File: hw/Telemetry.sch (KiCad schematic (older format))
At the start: 31 parts, among them J101 BOOT0, J102 BOOT0, J103 SPORT, J104 SBUS, J105 USB_B_Micro, J106 UART_EXP, SW101 SW_Push, U101 STM32F303CBx, U102 IS25LP032D, X101 SG-310_SCF_8.000000MHZ

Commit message: Updates to board revision 0.2 and newer HAL version
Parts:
- removed J101: BOOT0, Pin_Headers:Pin_Header_Straight_1x02_Pitch1.27mm, symbol Connector_Generic:Conn_01x02
- removed R104: 10k, Resistors_SMD:R_0603_HandSoldering, symbol Device:R_Small
- added R105: 1k5, digikey-footprints:0603, symbol Device:R_Small
- J106: footprint Pin_Headers:Pin_Header_Straight_1x04 -> Connector_PinSocket_1.27mm:PinSocket_1x04_P1.27mm_Vertical
- U101: symbol Misc:STM32F303CBx -> Telemetry-rescue:STM32F303CBx-Misc
- U102: symbol Misc:IS25LP032D -> Telemetry-rescue:IS25LP032D-Misc
- X101: symbol Misc:SG-310_SCF_8.000000MHZ -> Telemetry-rescue:SG-310_SCF_8.000000MHZ-Misc
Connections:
- net labels added: USB_ENUMRATION
- net labels removed: COOLING_TEMP, SERVO_3, SERVO_4
- wire segments 151 -> 149
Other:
- moved on the sheet: J105, J106

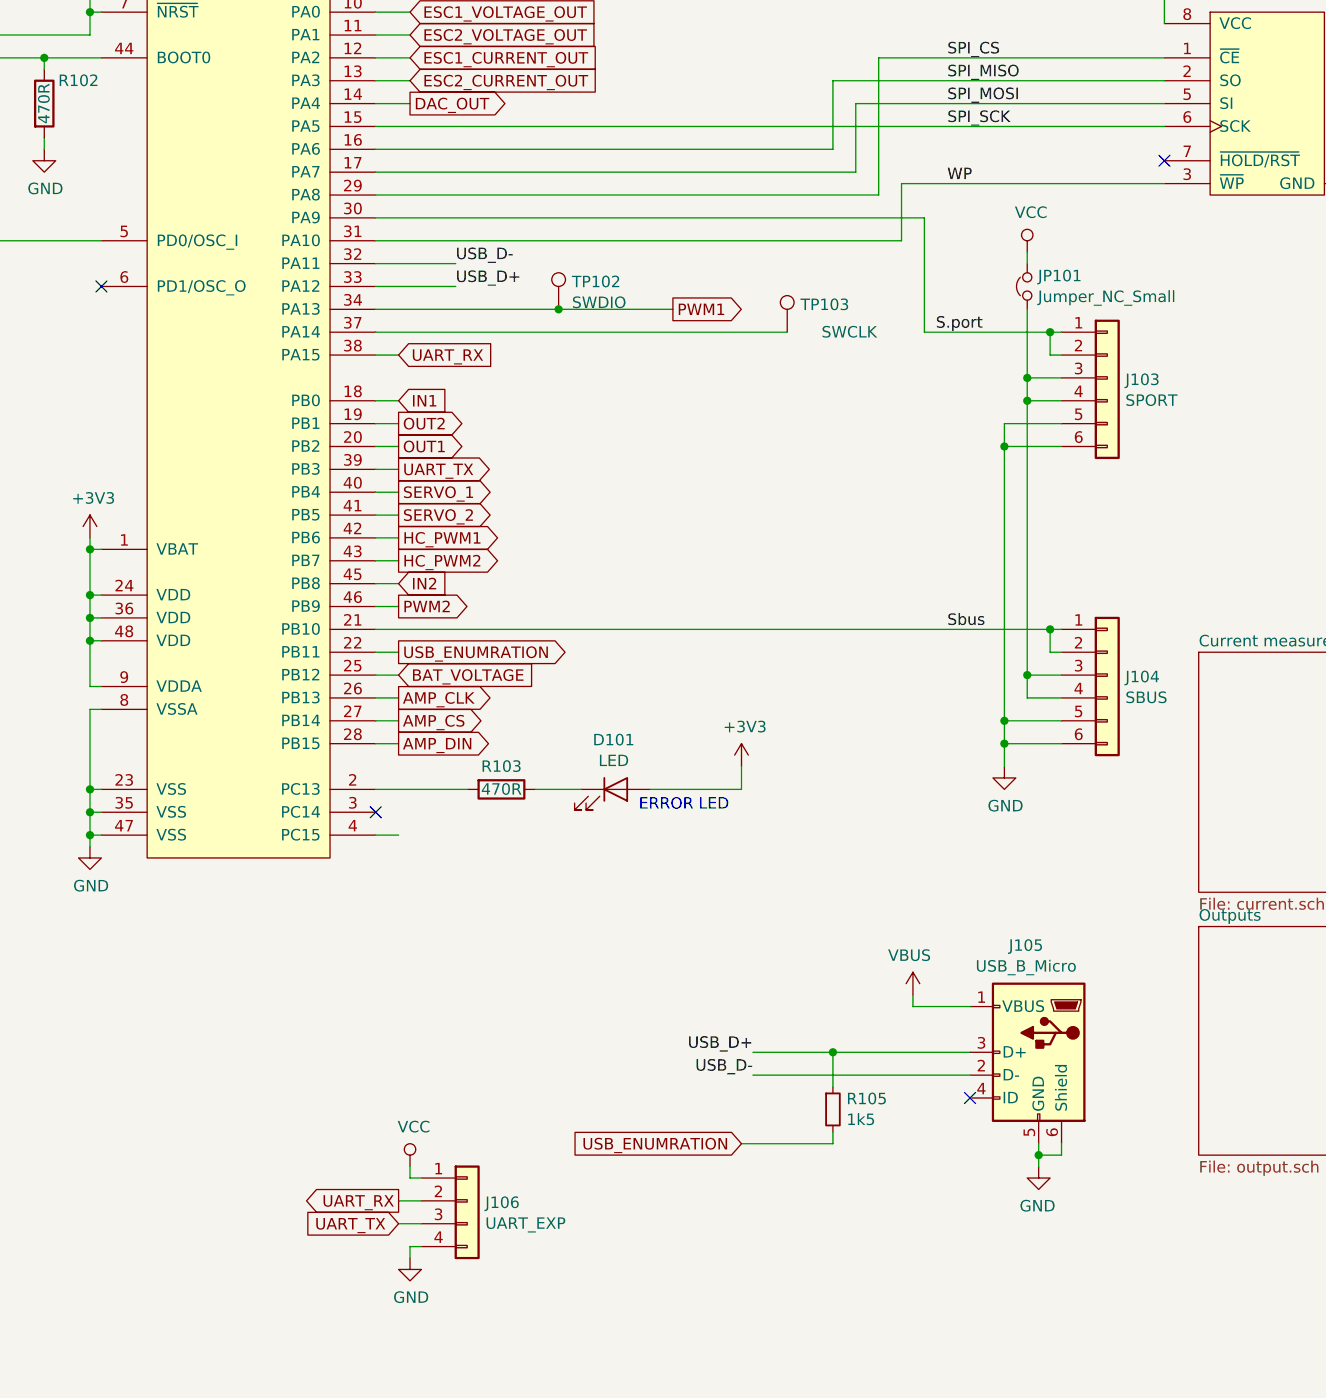
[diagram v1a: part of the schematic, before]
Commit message: Pin remapping and layout improvements
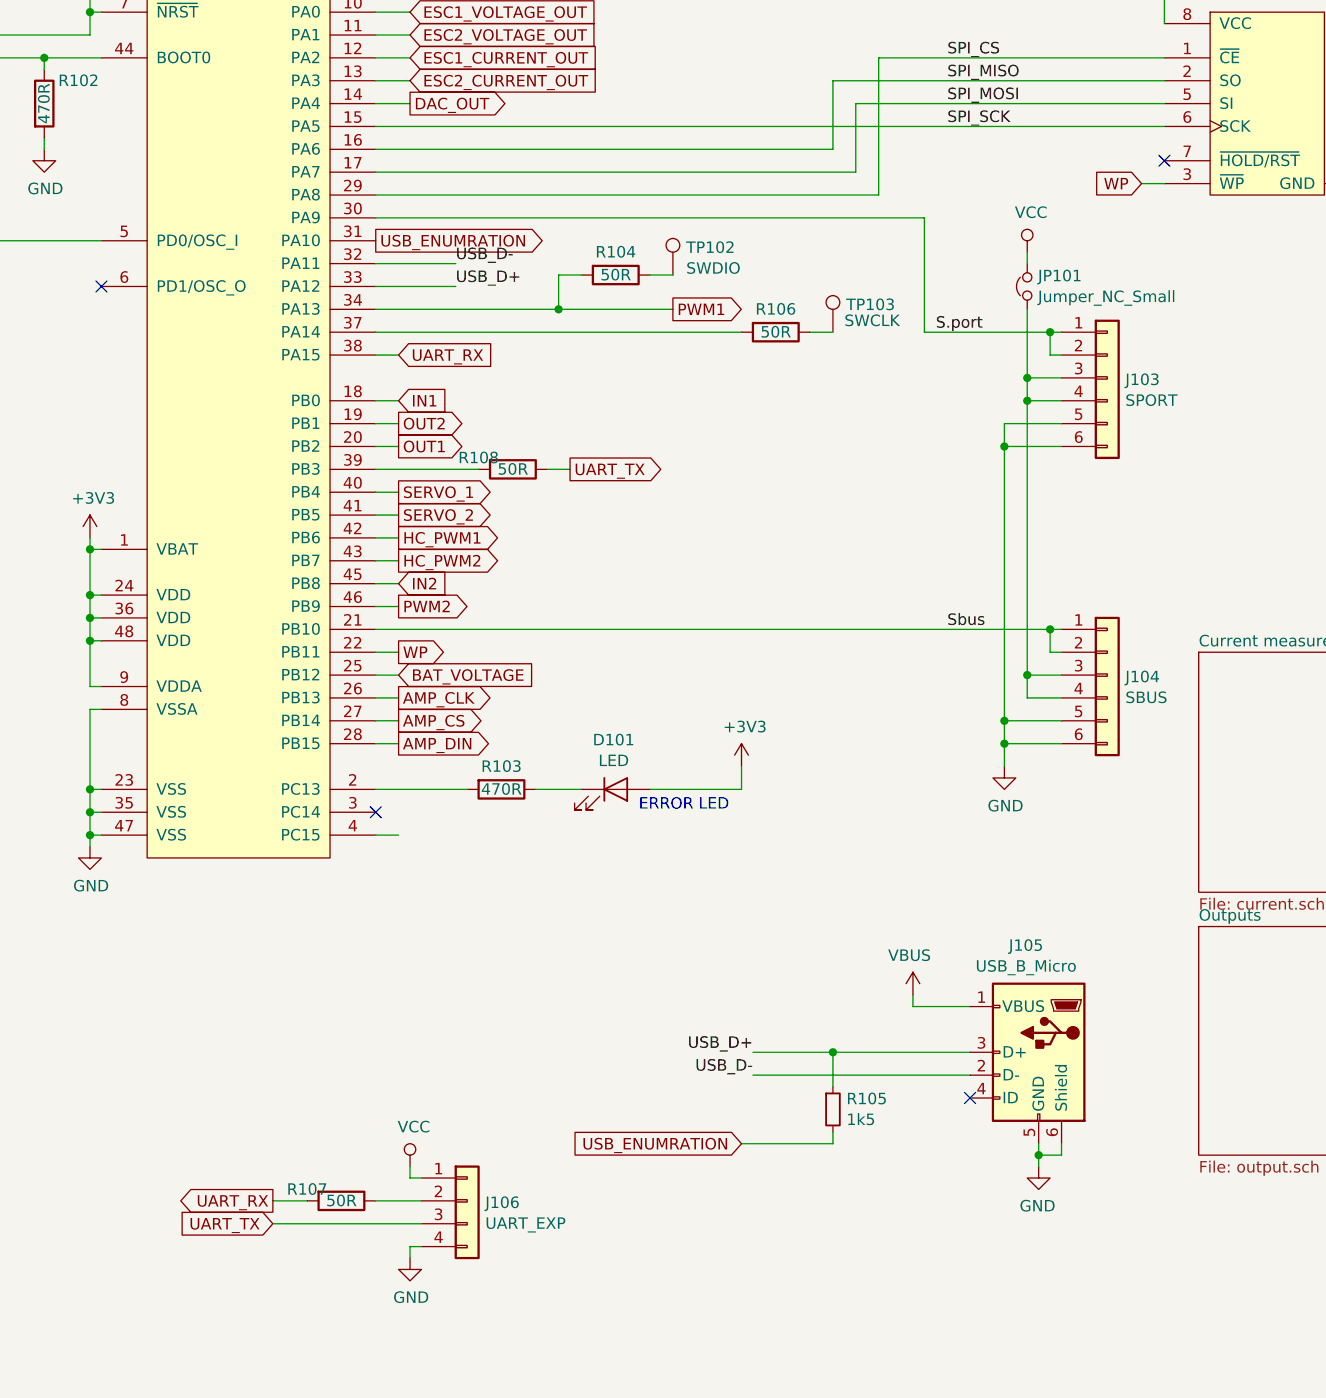
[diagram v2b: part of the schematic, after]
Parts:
- added R104, R106, R107, R108: 50R, Resistor_SMD:R_0603_1608Metric_Pad1.05x0.95mm_HandSolder, symbol Device:R
- C101, C102, C103, C104, C105, C106: footprint Capacitors_SMD:C_0603_HandSoldering -> Capacitor_SMD:C_0603_1608Metric_Pad1.05x0.95mm_HandSolder
- J106: footprint Connector_PinSocket_1.27mm:PinSocket_1x04_P1.27mm_Vertical -> Connector_PinHeader_2.54mm:PinHeader_2x02_P2.54mm_Vertical
- R101, R102, R103: footprint Resistors_SMD:R_0603_HandSoldering -> Resistor_SMD:R_0603_1608Metric_Pad1.05x0.95mm_HandSolder
- R105: footprint digikey-footprints:0603 -> Resistor_SMD:R_0603_1608Metric_Pad1.05x0.95mm_HandSolder
- SW101: footprint Pin_Headers:Pin_Header_Straight_1x02_Pitch1.27mm -> Button_Switch_SMD:SW_SPST_B3U-1000P
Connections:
- net PWM1: now also R104.2; no longer TP102.1
- net UART_RX: now also R107.2; no longer J106.2 (Pin_2)
- net UART_TX: now also R108.1; no longer U101.39 (PB3)
- net USB_ENUMRATION: now also U101.31 (PA10); no longer U101.22 (PB11)
- net WP: now also U101.22 (PB11); no longer U101.31 (PA10)
- net at U101.37 (PA14): now also R106.2; no longer TP103.1
- new net: R108.2, U101.39 (PB3)
- new net: J106.2 (Pin_2), R107.1
- new net: R104.1, TP102.1
- new net: R106.1, TP103.1
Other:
- moved on the sheet: TP102, TP103
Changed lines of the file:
@@
 F 0 "C102" H 792 7346 50  0000 L CNN
 F 1 "100n" H 792 7255 50  0000 L CNN
-F 2 "Capacitors_SMD:C_0603_HandSoldering" H 700 7300 50  0001 C CNN
+F 2 "Capacitor_SMD:C_0603_1608Metric_Pad1.05x0.95mm_HandSolder" H 700 7300 50  0001 C CNN
 F 3 "~" H 700 7300 50  0001 C CNN
 	1    700  7300
@@
 F 0 "C103" H 1192 7346 50  0000 L CNN
 F 1 "100n" H 1192 7255 50  0000 L CNN
-F 2 "Capacitors_SMD:C_0603_HandSoldering" H 1100 7300 50  0001 C CNN
+F 2 "Capacitor_SMD:C_0603_1608Metric_Pad1.05x0.95mm_HandSolder" H 1100 7300 50  0001 C CNN
 F 3 "~" H 1100 7300 50  0001 C CNN
 	1    1100 7300
@@
 F 0 "C104" H 1542 7346 50  0000 L CNN
 F 1 "100n" H 1542 7255 50  0000 L CNN
-F 2 "Capacitors_SMD:C_0603_HandSoldering" H 1450 7300 50  0001 C CNN
+F 2 "Capacitor_SMD:C_0603_1608Metric_Pad1.05x0.95mm_HandSolder" H 1450 7300 50  0001 C CNN
 F 3 "~" H 1450 7300 50  0001 C CNN
 	1    1450 7300
@@
 F 0 "C105" H 1892 7346 50  0000 L CNN
 F 1 "100n" H 1892 7255 50  0000 L CNN
-F 2 "Capacitors_SMD:C_0603_HandSoldering" H 1800 7300 50  0001 C CNN
+F 2 "Capacitor_SMD:C_0603_1608Metric_Pad1.05x0.95mm_HandSolder" H 1800 7300 50  0001 C CNN
 F 3 "~" H 1800 7300 50  0001 C CNN
 	1    1800 7300
@@
 F 0 "R101" V 3450 1100 50  0000 C CNN
 F 1 "10k" V 3550 1100 50  0000 C CNN
-F 2 "Resistors_SMD:R_0603_HandSoldering" V 3480 1100 50  0001 C CNN
+F 2 "Resistor_SMD:R_0603_1608Metric_Pad1.05x0.95mm_HandSolder" V 3480 1100 50  0001 C CNN
 F 3 "~" H 3550 1100 50  0001 C CNN
 	1    3550 1100
@@
 F 0 "R102" H 4750 1500 50  0000 C CNN
 F 1 "470R" V 4600 1400 50  0000 C CNN
-F 2 "Resistors_SMD:R_0603_HandSoldering" V 4530 1400 50  0001 C CNN
+F 2 "Resistor_SMD:R_0603_1608Metric_Pad1.05x0.95mm_HandSolder" V 4530 1400 50  0001 C CNN
 F 3 "~" H 4600 1400 50  0001 C CNN
 	1    4600 1400
@@
 F 0 "C101" H 3542 2296 50  0000 L CNN
 F 1 "100n" H 3542 2205 50  0000 L CNN
-F 2 "Capacitors_SMD:C_0603_HandSoldering" H 3450 2250 50  0001 C CNN
+F 2 "Capacitor_SMD:C_0603_1608Metric_Pad1.05x0.95mm_HandSolder" H 3450 2250 50  0001 C CNN
 F 3 "~" H 3450 2250 50  0001 C CNN
 	1    3450 2250
@@
 F 0 "SW101" H 4400 1135 50  0000 C CNN
 F 1 "SW_Push" H 4400 1044 50  0000 C CNN
-F 2 "Pin_Headers:Pin_Header_Straight_1x02_Pitch1.27mm" H 4400 1050 50  0001 C CNN
+F 2 "Button_Switch_SMD:SW_SPST_B3U-1000P" H 4400 1050 50  0001 C CNN
 F 3 "" H 4400 1050 50  0001 C CNN
 	1    4400 850
@@
 Text GLabel 6150 3600 2    50   Output ~ 0
 PWM2
-Wire Wire Line
-	7350 2300 6850 2300
 Text GLabel 6150 3300 2    50   Output ~ 0
 HC_PWM1
@@
 	6150 2900 6050 2900
 Wire Wire Line
-	6150 3000 6050 3000
-Wire Wire Line
 	6050 3100 6150 3100
 Wire Wire Line
@@
 Wire Wire Line
 	6150 4200 6050 4200
-Wire Wire Line
-	6250 6300 6150 6300
-Wire Wire Line
-	6150 6200 6250 6200
 $Comp
 L power:GND #PWR0122
@@
 F 0 "J106" H 6529 6192 50  0000 L CNN
 F 1 "UART_EXP" H 6529 6101 50  0000 L CNN
-F 2 "Connector_PinSocket_1.27mm:PinSocket_1x04_P1.27mm_Vertical" H 6450 6200 50  0001 C CNN
+F 2 "Connector_PinHeader_2.54mm:PinHeader_2x02_P2.54mm_Vertical" H 6450 6200 50  0001 C CNN
 F 3 "~" H 6450 6200 50  0001 C CNN
 	1    6450 6200
@@
 Wire Wire Line
 	8250 1200 8250 1800
-Wire Wire Line
-	6050 2400 7850 2400
 Connection ~ 9000 3700
 Wire Wire Line
@@
 	1    0    0    -1
 $EndComp
-Text Label 8550 1750 0    50   ~ 0
-WP
 NoConn ~ 9500 1650
 $Comp
@@
 F 0 "R103" V 6500 4400 50  0000 C CNN
 F 1 "470R" V 6600 4400 50  0000 C CNN
-F 2 "Resistors_SMD:R_0603_HandSoldering" V 6530 4400 50  0001 C CNN
+F 2 "Resistor_SMD:R_0603_1608Metric_Pad1.05x0.95mm_HandSolder" V 6530 4400 50  0001 C CNN
 F 3 "~" H 6600 4400 50  0001 C CNN
 	1    6600 4400
@@
 F 0 "C106" H 10492 1446 50  0000 L CNN
 F 1 "100n" H 10492 1355 50  0000 L CNN
-F 2 "Capacitors_SMD:C_0603_HandSoldering" H 10400 1400 50  0001 C CNN
+F 2 "Capacitor_SMD:C_0603_1608Metric_Pad1.05x0.95mm_HandSolder" H 10400 1400 50  0001 C CNN
 F 3 "~" H 10400 1400 50  0001 C CNN
 	1    10400 1400
@@
 	6050 1500 9500 1500
 Wire Wire Line
-	9500 1750 8350 1750
-Wire Wire Line
-	6050 2000 8350 2000
-Wire Wire Line
-	8350 2000 8350 1750
+	9500 1750 9400 1750
 $Comp
 L Mechanical:MountingHole MH101
@@
 Wire Wire Line
 	6050 4600 6150 4600
-Connection ~ 6850 2300
-Wire Wire Line
-	6850 2300 6050 2300
 $Comp
 L Connector:TestPoint TP101
@@
 L Connector:TestPoint TP102
 U 1 1 5CECADFA
-P 6850 2300
-F 0 "TP102" H 6908 2420 50  0000 L CNN
-F 1 "SWDIO" H 6908 2329 50  0000 L CNN
-F 2 "Wire_Pads:SolderWirePad_single_0-8mmDrill" H 7050 2300 50  0001 C CNN
-F 3 "~" H 7050 2300 50  0001 C CNN
-	1    6850 2300
+P 7350 2150
+F 0 "TP102" H 7408 2270 50  0000 L CNN
+F 1 "SWDIO" H 7408 2179 50  0000 L CNN
+F 2 "Wire_Pads:SolderWirePad_single_0-8mmDrill" H 7550 2150 50  0001 C CNN
+F 3 "~" H 7550 2150 50  0001 C CNN
+	1    7350 2150
 	1    0    0    -1
 $EndComp
@@
 L Connector:TestPoint TP103
 U 1 1 5CECB040
-P 7850 2400
-F 0 "TP103" H 7908 2520 50  0000 L CNN
-F 1 "SWCLK" H 8000 2400 50  0000 L CNN
-F 2 "Wire_Pads:SolderWirePad_single_0-8mmDrill" H 8050 2400 50  0001 C CNN
-F 3 "~" H 8050 2400 50  0001 C CNN
-	1    7850 2400
-	1    0    0    -1
-$EndComp
-Text GLabel 6150 6200 0    50   Output ~ 0
+P 8050 2400
+F 0 "TP103" H 8108 2520 50  0000 L CNN
+F 1 "SWCLK" H 8100 2450 50  0000 L CNN
+F 2 "Wire_Pads:SolderWirePad_single_0-8mmDrill" H 8250 2400 50  0001 C CNN
+F 3 "~" H 8250 2400 50  0001 C CNN
+	1    8050 2400
+	1    0    0    -1
+$EndComp
+Text GLabel 5600 6200 0    50   Output ~ 0
 UART_RX
-Text GLabel 6150 6300 0    50   Input ~ 0
+Text GLabel 5600 6300 0    50   Input ~ 0
 UART_TX
 Text GLabel 6150 3100 2    50   Output ~ 0
@@
 Text GLabel 6150 3200 2    50   Output ~ 0
 SERVO_2
-Text GLabel 6150 3800 2    50   Output ~ 0
+Text GLabel 6050 2000 2    50   Output ~ 0
 USB_ENUMRATION
 Wire Wire Line
@@
 F 0 "R105" H 8109 5846 50  0000 L CNN
 F 1 "1k5" H 8109 5755 50  0000 L CNN
-F 2 "digikey-footprints:0603" H 8050 5800 50  0001 C CNN
+F 2 "Resistor_SMD:R_0603_1608Metric_Pad1.05x0.95mm_HandSolder" H 8050 5800 50  0001 C CNN
 F 3 "~" H 8050 5800 50  0001 C CNN
 	1    8050 5800
@@
 Text GLabel 6150 2500 2    50   Input ~ 0
 UART_RX
-Text GLabel 6150 3000 2    50   Output ~ 0
+Text GLabel 6900 3000 2    50   Output ~ 0
 UART_TX
+Text GLabel 9400 1750 0    50   Input ~ 0
+WP
+Text GLabel 6150 3800 2    50   Output ~ 0
+WP
+$Comp
+L Device:R R104
+U 1 1 5E4C8C09
+P 7100 2150
+F 0 "R104" V 7000 2150 50  0000 C CNN
+F 1 "50R" V 7100 2150 50  0000 C CNN
+F 2 "Resistor_SMD:R_0603_1608Metric_Pad1.05x0.95mm_HandSolder" V 7030 2150 50  0001 C CNN
+F 3 "~" H 7100 2150 50  0001 C CNN
+	1    7100 2150
+	0    1    1    0
+$EndComp
+Wire Wire Line
+	7250 2150 7350 2150
+Wire Wire Line
+	6050 2300 6850 2300
+Wire Wire Line
+	6950 2150 6850 2150
+Wire Wire Line
+	6850 2150 6850 2300
+Connection ~ 6850 2300
+Wire Wire Line
+	6850 2300 7350 2300
+$Comp
+L Device:R R106
+U 1 1 5E4D66BC
+P 7800 2400
+F 0 "R106" V 7700 2400 50  0000 C CNN
+F 1 "50R" V 7800 2400 50  0000 C CNN
+F 2 "Resistor_SMD:R_0603_1608Metric_Pad1.05x0.95mm_HandSolder" V 7730 2400 50  0001 C CNN
+F 3 "~" H 7800 2400 50  0001 C CNN
+	1    7800 2400
+	0    1    1    0
+$EndComp
+Wire Wire Line
+	8050 2400 7950 2400
+Wire Wire Line
+	6050 2400 7650 2400
+$Comp
+L Device:R R107
+U 1 1 5E51659E
+P 5900 6200
+F 0 "R107" V 5850 6050 50  0000 C CNN
+F 1 "50R" V 5900 6200 50  0000 C CNN
+F 2 "Resistor_SMD:R_0603_1608Metric_Pad1.05x0.95mm_HandSolder" V 5830 6200 50  0001 C CNN
+F 3 "~" H 5900 6200 50  0001 C CNN
+	1    5900 6200
+	0    1    1    0
+$EndComp
+Wire Wire Line
+	5750 6200 5600 6200
+Wire Wire Line
+	6050 6200 6250 6200
+$Comp
+L Device:R R108
+U 1 1 5E517A65
+P 6650 3000
+F 0 "R108" V 6600 2850 50  0000 C CNN
+F 1 "50R" V 6650 3000 50  0000 C CNN
+F 2 "Resistor_SMD:R_0603_1608Metric_Pad1.05x0.95mm_HandSolder" V 6580 3000 50  0001 C CNN
+F 3 "~" H 6650 3000 50  0001 C CNN
+	1    6650 3000
+	0    1    1    0
+$EndComp
+Wire Wire Line
+	6800 3000 6900 3000
+Wire Wire Line
+	6050 3000 6500 3000
+Wire Wire Line
+	5600 6300 6250 6300
 $EndSCHEMATC
